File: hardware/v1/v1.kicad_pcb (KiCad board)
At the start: 2 copper layers, 54 x 86 mm, 38 parts, among them J1 FPC 24P 0.5mm bottom contact, K1 GND, K2 DN_RX, K3 DN_TX, K4 DN_DET, K5 GND, M1 5x2 mm disc, M2 5x2 mm disc, M3 5x2 mm disc, M4 5x2 mm disc, P1 GND, P2 UP_TX, P3 UP_RX, P4 GND, P5 UP_DET, Q1 AO3400A, SW1 power, SW2 A: next, SW3 B: confirm, U1 Raspberry Pi Pico 2 (no heade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

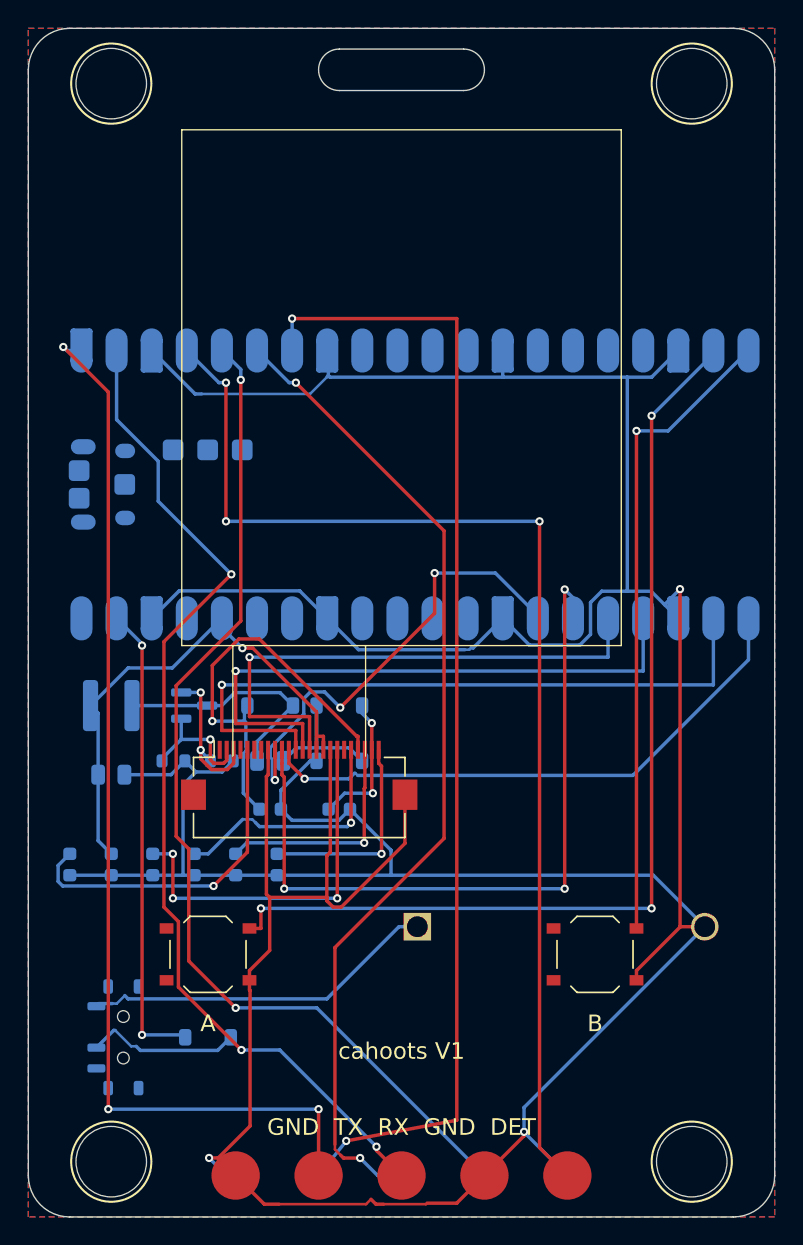
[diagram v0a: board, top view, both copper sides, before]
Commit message: V1: a 3D model for the panel, a hero render of both sides, tracks kept at the fab's width floor
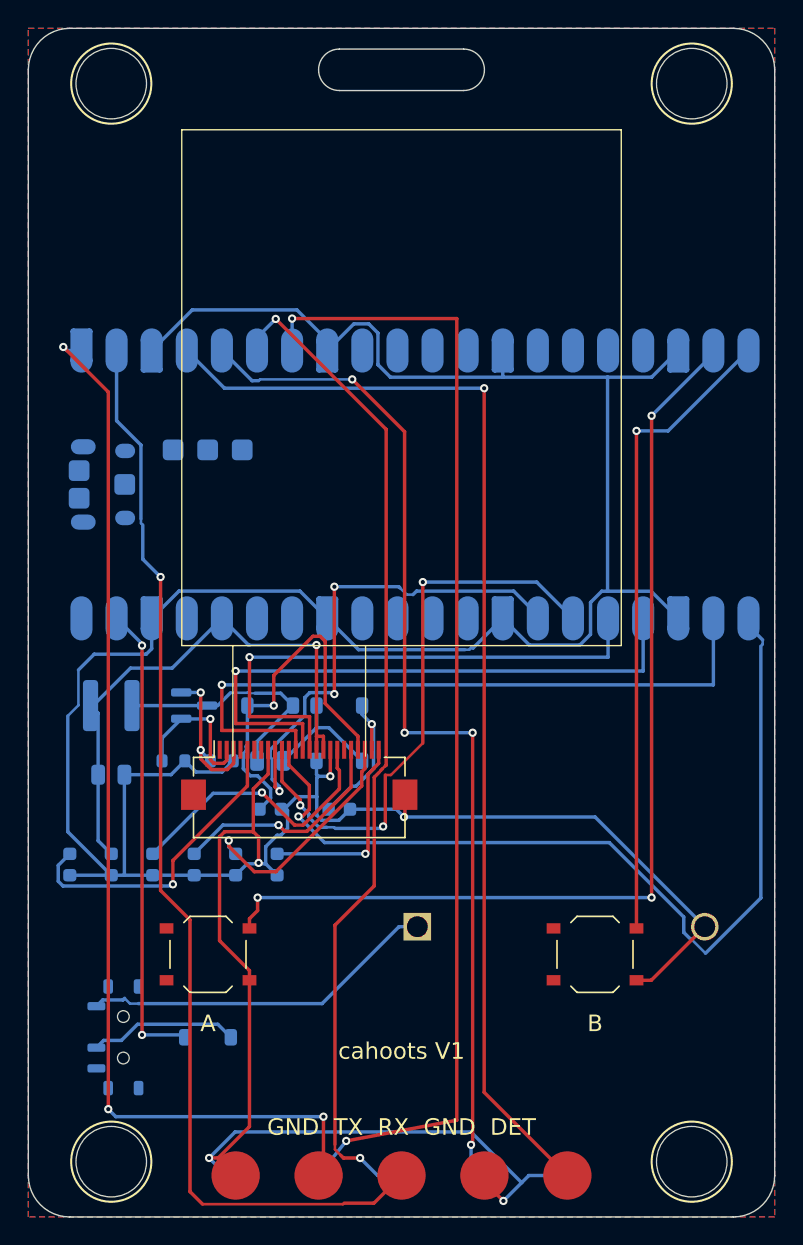
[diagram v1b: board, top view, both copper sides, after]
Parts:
- added DS1: GDEY0154D67, cahoots:Panel_GDEY0154D67, F.Cu at (100.0, 83.0)
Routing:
- net GND: track 331.7 -> 294.5 mm, vias 3 -> 5
- net EPD_DC: track 41.4 -> 66.5 mm
- net EPD_RST: track 54.4 -> 42.5 mm
- net VDD: track 27.3 -> 20.3 mm, vias 3 -> 1
- net UP_RX: track 73.9 -> 79.6 mm, vias 3 -> 1
- net EPD_BUSY: track 34.2 -> 37.3 mm
- net VGH: track 29.8 -> 27.0 mm
- net 3V3: track 37.5 -> 40.1 mm
- net UP_DET: track 84.7 -> 82.1 mm, vias 3 -> 1
- net VSH2: track 24.6 -> 22.8 mm
- net VSH1: track 18.0 -> 16.4 mm
- net GDR: track 9.34 -> 10.8 mm
- net VGL: track 10.3 -> 11.2 mm, vias 2 -> 1
- net VSL: track 16.4 -> 17.3 mm
- net VCOM: track 15.2 -> 14.3 mm
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
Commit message: V1: the Cahoots mark on the silkscreen, small by the name on the front and full size on the back; hero.sh renders the two-sided view
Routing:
- net EPD_DC: track 66.5 -> 42.7 mm
- net VSL: track 17.3 -> 25.8 mm, vias 1 -> 3
- net VGH: track 27.0 -> 19.7 mm
- net EPD_BUSY: track 37.3 -> 44.3 mm
- net VSH1: track 16.4 -> 22.0 mm, vias 1 -> 3
- net UP_RX: track 79.6 -> 74.8 mm, vias 1 -> 3
- net GND: track 294.5 -> 299.0 mm, vias 5 -> 4
- net DN_TX: track 73.4 -> 77.3 mm, vias 2 -> 4
- net EPD_RST: track 42.5 -> 39.7 mm
- net VGL: track 11.2 -> 14.0 mm, vias 1 -> 2
- net DN_DET: track 74.9 -> 77.4 mm
- net VSH2: track 22.8 -> 24.5 mm
- net BTN_A: track 72.4 -> 74.2 mm
- net GDR: track 10.8 -> 9.34 mm
- net UP_DET: track 82.1 -> 83.5 mm, vias 1 -> 3
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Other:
- board text added: "V1"
- board text added: "cahoots"
- board text removed: "cahoots V1"

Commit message: V1 case: a tray and a lid that click together, generated from the design table; panel flush in the lid; hero shows the badge in its case
case.py (CadQuery) writes STEP and STL for printing and transparent WRL for KiCad's 3D view.
Snap tabs on the lid's skirt into windows in the tray's wall; magnet pockets, pad funnels,
button holes, USB notch, lanyard slot. The pile-contact reach is written up as the open
question, with raised pads as the plan.
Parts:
- added CASE1: tray and lid, cahoots:Case, F.Cu at (100.0, 100.0)
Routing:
- net GND: track 299.0 -> 314.1 mm, vias 4 -> 3
- net VSH1: track 22.0 -> 34.4 mm
- net VSL: track 25.8 -> 16.3 mm, vias 3 -> 1
- net DN_DET: track 77.4 -> 68.9 mm, vias 4 -> 2
- net VDD: track 20.0 -> 26.5 mm
- net EPD_BUSY: track 44.3 -> 38.0 mm
- net UP_RX: track 74.8 -> 80.8 mm
- net DN_TX: track 77.3 -> 83.0 mm, vias 4 -> 2
- net VGH: track 19.7 -> 16.0 mm
- net N2: track 9.46 -> 13.1 mm
- net UP_TX: track 79.3 -> 75.8 mm
- net UP_DET: track 83.5 -> 86.7 mm
- net VSH2: track 24.5 -> 27.6 mm
- net SW: track 17.5 -> 19.4 mm
- net EPD_DC: track 42.7 -> 41.6 mm
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
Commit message: V1: JST-SH UP and DN ports replace the pads and spring pins; cable openings in the case; switch and cell holder models; a sheet of each piece front and back
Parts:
- removed K1, K5: GND, cahoots:Pogo_SMD_D2.4mm
- removed K2: DN_RX, cahoots:Pogo_SMD_D2.4mm
- removed K3: DN_TX, cahoots:Pogo_SMD_D2.4mm
- removed K4: DN_DET, cahoots:Pogo_SMD_D2.4mm
- removed P1, P4: GND, cahoots:Pad_D3.5mm
- removed P2: UP_TX, cahoots:Pad_D3.5mm
- removed P3: UP_RX, cahoots:Pad_D3.5mm
- removed P5: UP_DET, cahoots:Pad_D3.5mm
- added J2: UP port, JST-SH 4, JST_SH_SM04B-SRSS-TB_1x04-1MP_P1.00mm_Horizontal, F.Cu at (113.0, 139.5)
- added J3: DN port, JST-SH 4, JST_SH_SM04B-SRSS-TB_1x04-1MP_P1.00mm_Horizontal, F.Cu at (87.0, 139.5)
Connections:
- U1 pad 4: UP_DET -> (no net)
- U1 pad 5: DN_DET -> (no net)
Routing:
- net UP_DET: track 86.7 -> 0.00 mm, vias 3 -> 0
- net DN_DET: track 68.9 -> 0.00 mm, vias 2 -> 0
- net UP_TX: track 75.8 -> 93.3 mm, vias 3 -> 1
- net GND: track 314.1 -> 297.4 mm
- net VSH1: track 34.4 -> 18.7 mm, vias 3 -> 1
- net DN_RX: track 83.6 -> 71.2 mm, vias 2 -> 1
- net UP_RX: track 80.8 -> 91.9 mm, vias 3 -> 1
- net DN_TX: track 83.0 -> 72.6 mm, vias 2 -> 1
- net VDD: track 26.5 -> 18.3 mm, vias 3 -> 1
- net BTN_A: track 73.9 -> 66.4 mm
- net EPD_RST: track 40.1 -> 45.7 mm
- net RESE: track 10.3 -> 14.9 mm
- net EPD_DC: track 41.6 -> 45.2 mm
- net N2: track 13.1 -> 9.78 mm
- net VGH: track 16.0 -> 18.7 mm
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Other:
- board text added: "DN"
- board text added: "UP"
- board text removed: "GND TX RX GND DET"

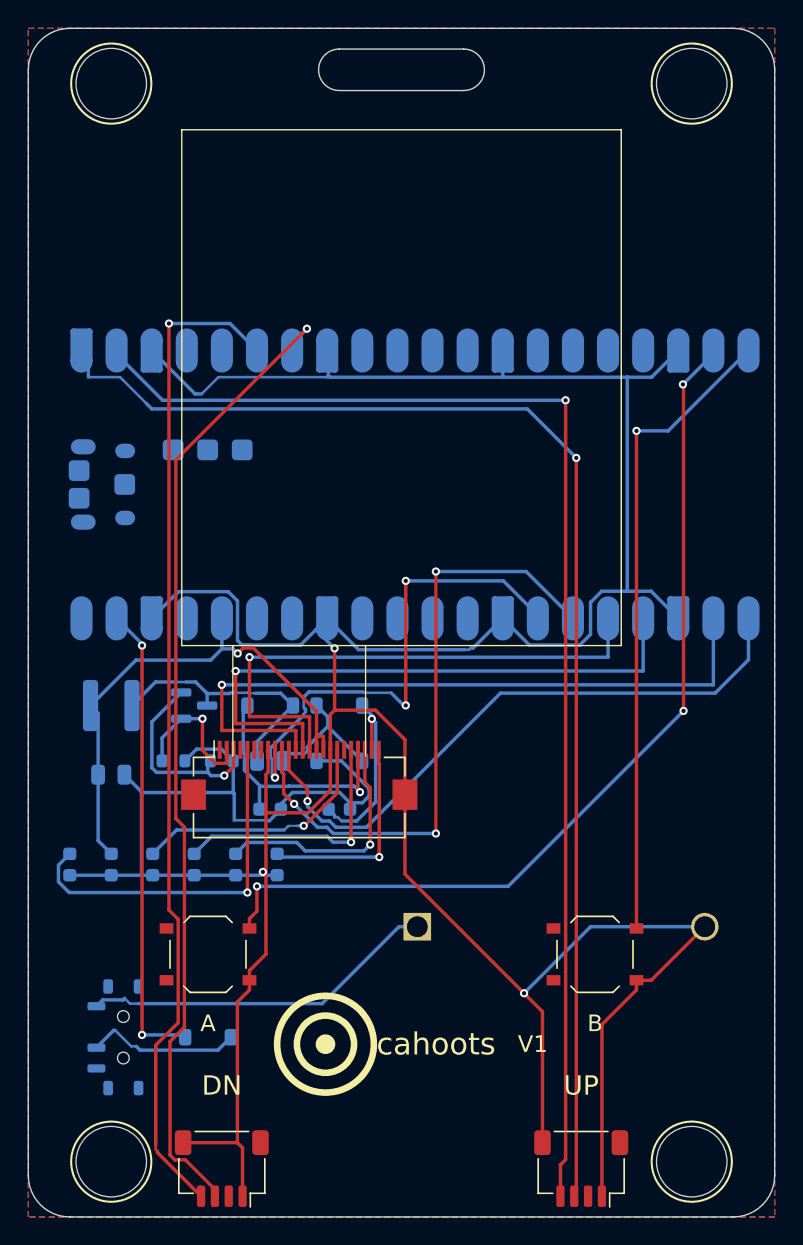
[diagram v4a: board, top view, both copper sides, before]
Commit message: V1: magnetic pogo pair at both ends (Adafruit 5359), faces flush with the case; JST sockets moved beside it; lanyard slot gone; round models as face sets so magnets, cell and pins render; end view on the assembly sheet
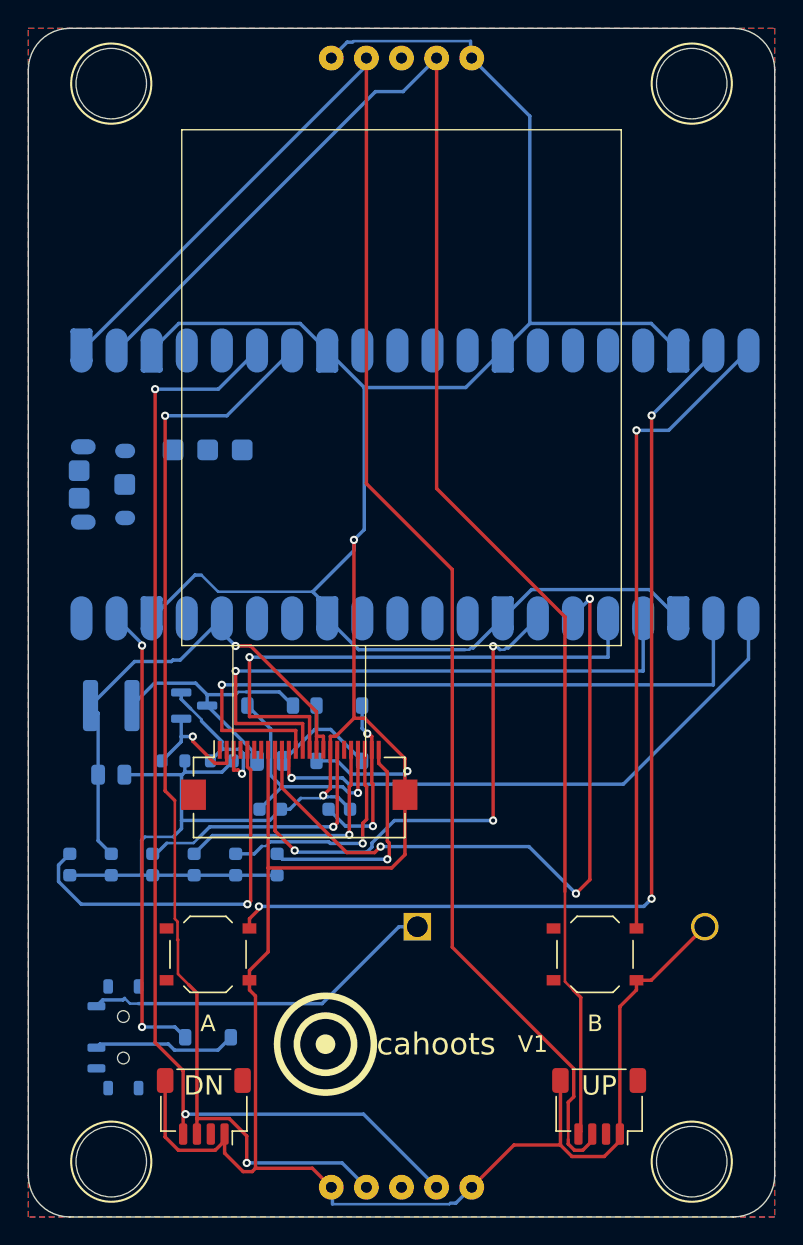
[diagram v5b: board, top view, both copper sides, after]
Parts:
- added J4: UP, magnetic pads, cahoots:Pogo_MG05254_RA_1x05, F.Cu at (100.0, 59.1)
- added J5: DN, magnetic pins, cahoots:Pogo_MG05254_RA_1x05, F.Cu at (100.0, 140.8)
- moved J2 4.68 mm to (114.3, 135.0)
- moved J3 4.68 mm to (85.7, 135.0)
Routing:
- net GND: track 297.4 -> 332.3 mm
- net UP_TX: track 93.3 -> 117.3 mm, vias 1 -> 0
- net UP_RX: track 91.9 -> 114.2 mm, vias 1 -> 0
- net DN_TX: track 72.6 -> 83.8 mm, vias 1 -> 2
- net DN_RX: track 71.2 -> 79.5 mm, vias 1 -> 2
- net BTN_A: track 66.4 -> 72.0 mm
- net EPD_RST: track 45.7 -> 51.2 mm
- net EPD_BUSY: track 36.9 -> 40.3 mm
- net EPD_DC: track 45.2 -> 42.1 mm
- net RESE: track 14.9 -> 11.9 mm
- net GDR: track 10.6 -> 8.89 mm
- net VSH2: track 26.7 -> 28.1 mm
- net VDD: track 18.3 -> 19.6 mm
- net VGL: track 14.0 -> 12.8 mm, vias 1 -> 2
- net VCOM: track 15.3 -> 16.4 mm
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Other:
- outline, holes or cut-outs redrawn

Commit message: V1: stack face to face. Straight magnetic pogo pair (Adafruit 5413): pin half on the board, pins up through the lid; pad half flush in the tray floor on a pigtail to DN. Lid cavity 2.2, badge 13.4 mm; skirt down to snaps below the board; stacked view on the sheet
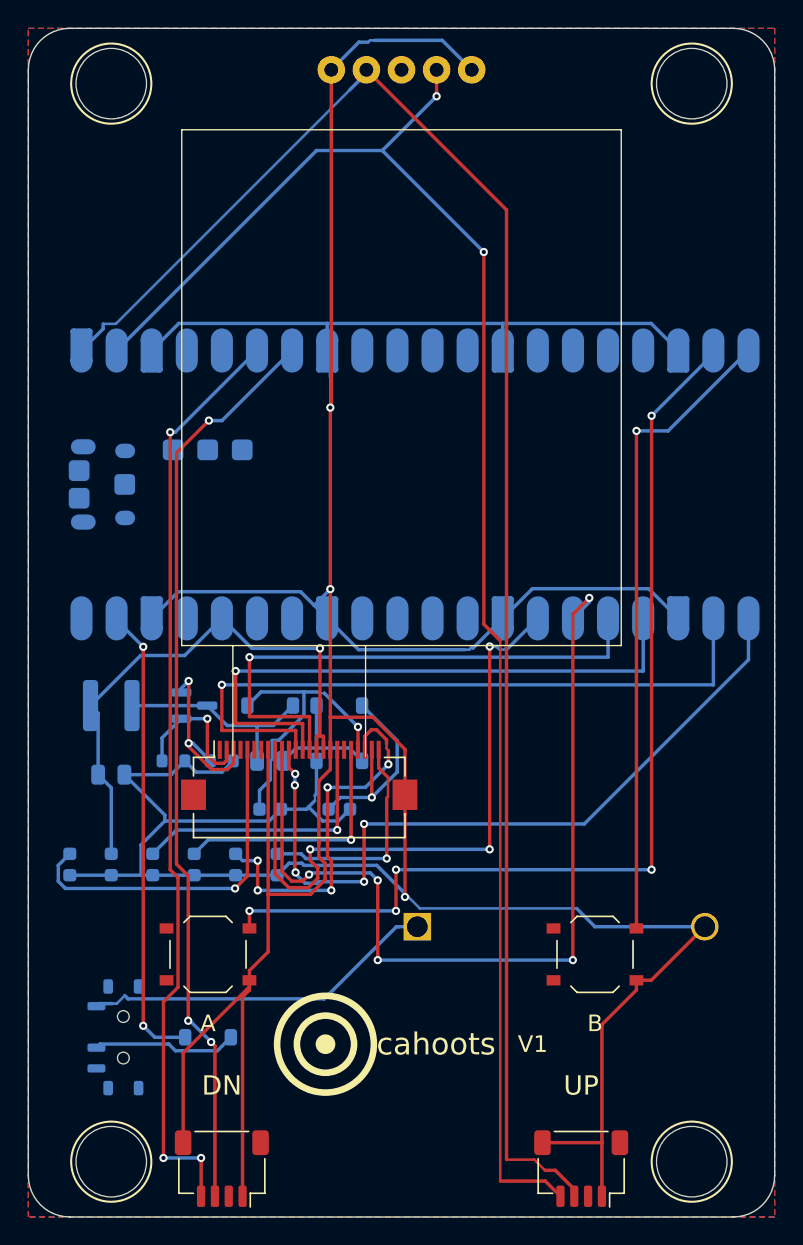
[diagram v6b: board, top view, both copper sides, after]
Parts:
- removed J5: DN, magnetic pins, cahoots:Pogo_MG05254_RA_1x05
- added P1: DN, magnetic pads, in the tray floor, cahoots:Pogo_MG005_tray, F.Cu at (100.0, 59.6)
- J4: value UP, magnetic pads -> UP, magnetic pogo pins; footprint cahoots:Pogo_MG05254_RA_1x05 -> cahoots:Pogo_MG005_1x05
- moved J2 4.68 mm to (113.0, 139.5)
- moved J3 4.68 mm to (87.0, 139.5)
- moved J4 0.85 mm to (100.0, 60.0)
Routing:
- net DN_TX: track 83.8 -> 67.4 mm, vias 2 -> 3
- net EPD_RST: track 51.2 -> 65.0 mm, vias 3 -> 5
- net DN_RX: track 79.5 -> 66.4 mm, vias 2 -> 3
- net EPD_DC: track 42.1 -> 54.4 mm, vias 1 -> 5
- net GND: track 332.3 -> 344.1 mm
- net VSL: track 16.5 -> 26.8 mm, vias 1 -> 5
- net EPD_BUSY: track 40.3 -> 47.3 mm
- net SW: track 19.4 -> 15.4 mm
- net VGH: track 18.0 -> 21.2 mm
- net 3V3: track 37.6 -> 40.3 mm
- net VGL: track 12.8 -> 15.4 mm, vias 2 -> 1
- net VSH2: track 28.1 -> 25.7 mm
- net GDR: track 8.89 -> 10.7 mm
- net UP_RX: track 114.2 -> 115.6 mm, vias 0 -> 2
- net UP_TX: track 117.3 -> 118.7 mm
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
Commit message: V1: the stand-in cell holder model sits on the BS-07 footprint's cell outline
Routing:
- net GND: track 344.1 -> 313.0 mm, vias 3 -> 4
- net EPD_RST: track 65.0 -> 37.8 mm, vias 5 -> 3
- net EPD_DC: track 54.4 -> 41.1 mm, vias 5 -> 1
- net VSL: track 26.8 -> 16.1 mm, vias 5 -> 1
- net VSH1: track 18.3 -> 27.9 mm, vias 1 -> 3
- net EPD_BUSY: track 47.3 -> 40.9 mm
- net UP_TX: track 118.7 -> 124.5 mm
- net VGH: track 21.2 -> 26.9 mm
- net VGL: track 15.4 -> 20.4 mm
- net SW: track 15.4 -> 17.7 mm
- net DN_RX: track 66.4 -> 68.4 mm, vias 3 -> 1
- net VCOM: track 16.3 -> 14.7 mm
- net DN_TX: track 67.4 -> 66.1 mm, vias 3 -> 1
- net RESE: track 13.0 -> 11.8 mm
- net UP_RX: track 115.6 -> 116.8 mm, vias 2 -> 0
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
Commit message: V1: regenerated with J5 (Qwiic, bottom centre) and J6 (2x5 header, back at -5,-30); 0 incomplete, 0 DRC; render scripts use web/ for Playwright
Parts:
- added J5: Qwiic / STEMMA QT, JST-SH 4, JST_SH_SM04B-SRSS-TB_1x04-1MP_P1.00mm_Horizontal, F.Cu at (100.0, 139.5)
- added J6: spare GPIO, 2x5, PinHeader_2x05_P2.54mm_Vertical, B.Cu at (93.7, 135.1)
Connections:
- U1 pad 10: (no net) -> GP7
- U1 pad 11: (no net) -> I2C_SDA
- U1 pad 12: (no net) -> I2C_SCL
- U1 pad 14: (no net) -> GP10
- U1 pad 15: (no net) -> GP11
- U1 pad 16: (no net) -> GP12
- U1 pad 17: (no net) -> GP13
- U1 pad 29: (no net) -> GP22
- U1 pad 31: (no net) -> GP26
- U1 pad 9: (no net) -> GP6
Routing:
- net I2C_SCL: track 0.00 -> 79.0 mm, vias 0 -> 5
- net I2C_SDA: track 0.00 -> 78.1 mm, vias 0 -> 5
- net GP6: track 0.00 -> 69.6 mm, vias 0 -> 2
- net GP12: track 0.00 -> 66.8 mm, vias 0 -> 2
- net GP7: track 0.00 -> 58.7 mm, vias 0 -> 1
- net GP13: track 0.00 -> 58.7 mm, vias 0 -> 1
- net GP10: track 0.00 -> 57.9 mm, vias 0 -> 1
- net GP11: track 0.00 -> 56.4 mm, vias 0 -> 1
- net 3V3: track 40.3 -> 80.5 mm
- net GP26: track 0.00 -> 37.0 mm, vias 0 -> 1
- net GND: track 313.0 -> 348.4 mm, vias 4 -> 6
- net GP22: track 0.00 -> 32.8 mm, vias 0 -> 1
- net EPD_BUSY: track 40.9 -> 52.4 mm, vias 3 -> 5
- net VSH1: track 27.9 -> 18.6 mm
- net VCOM: track 14.7 -> 23.0 mm, vias 1 -> 3
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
